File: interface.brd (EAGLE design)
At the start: 101.6 x 38.1 mm, 13 parts, among them U1 LCD-16X2

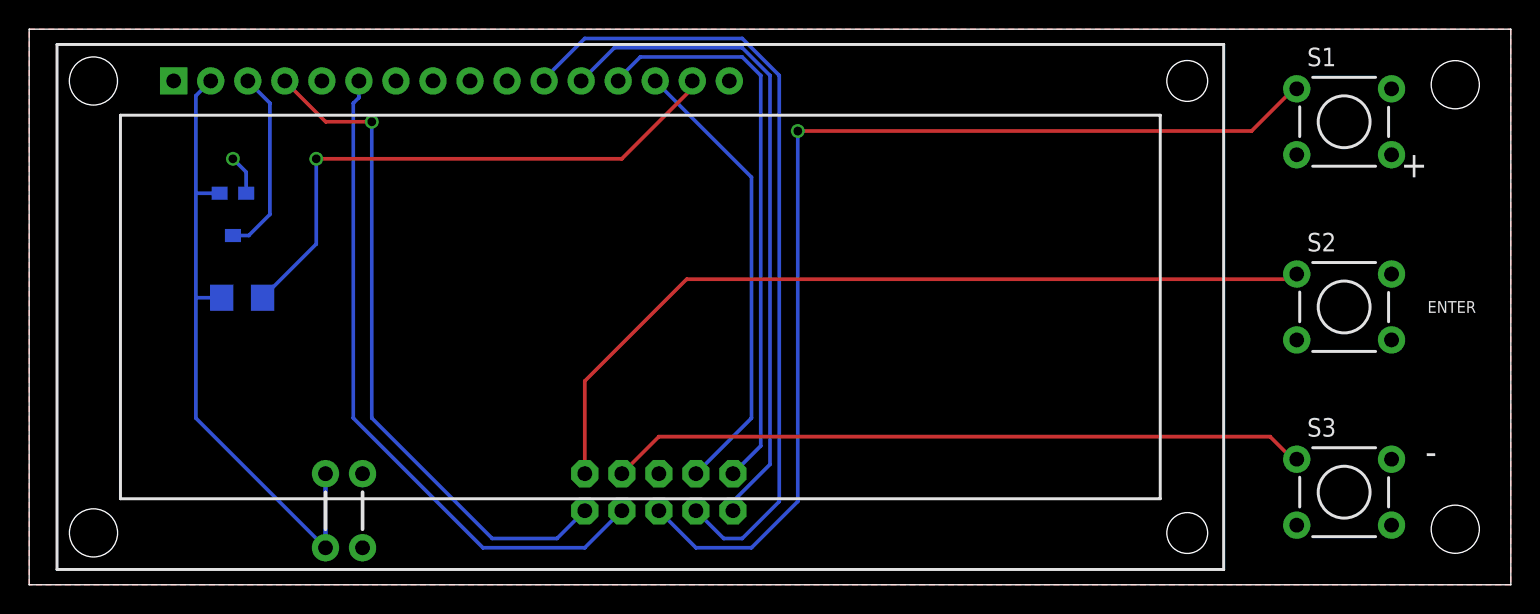
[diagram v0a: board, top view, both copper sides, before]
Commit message: Cleaning up DRC issues
Sparkfun package TRIMPOT_TC33 had issues with silkscreen.  SS from LCD was passing over some pads.  Switched LCD ss to tDocu and cleaned up ss lines on trimpot so they no longer overlapped the pads.
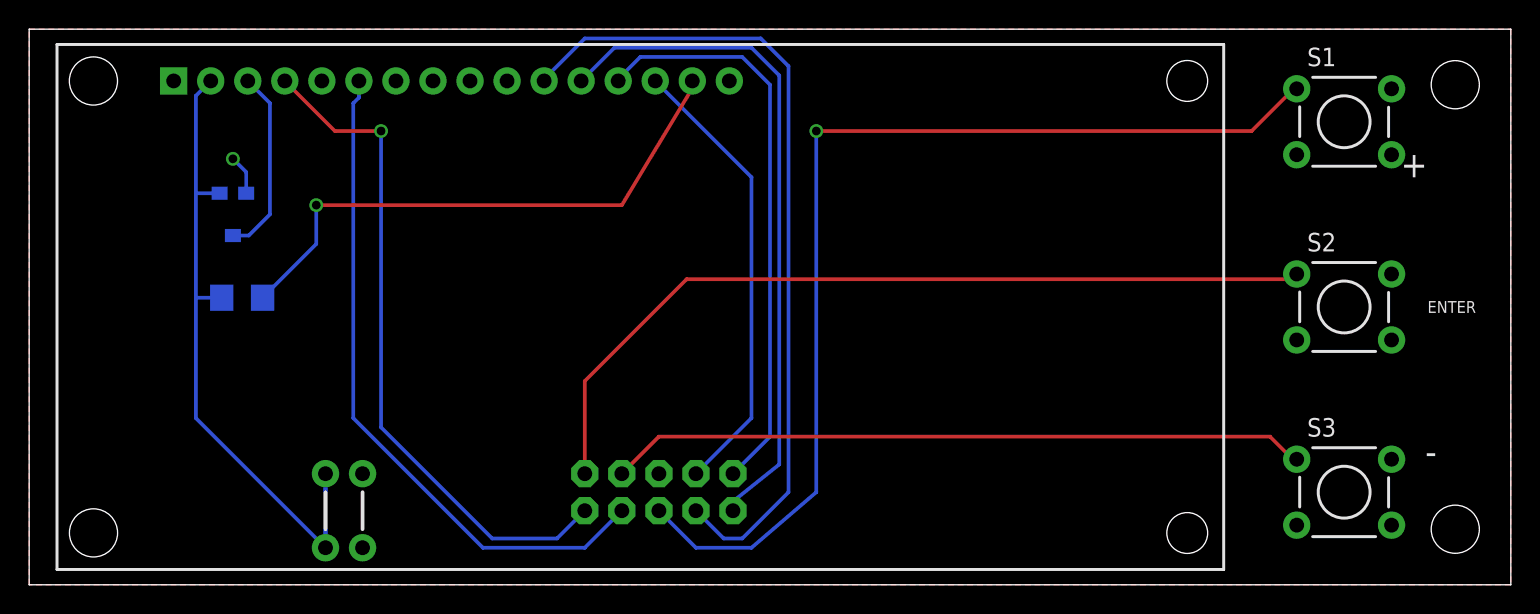
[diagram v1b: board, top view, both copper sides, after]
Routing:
- net LCD_DB4: track 55.2 -> 56.5 mm
- net LCD_DB5: track 45.6 -> 46.7 mm
- net N$1: track 39.3 -> 38.7 mm
- net BTN0: track 72.7 -> 72.2 mm
- net LCD_DB6: track 39.1 -> 39.7 mm
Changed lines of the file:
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@@
 </variantdefs>
 <classes>
-<class number="0" name="default" width="0" drill="0">
+<class number="0" name="default" width="0.254" drill="0.508">
+<clearance class="0" value="0.254"/>
 </class>
 </classes>
@@
 <wire x1="40.39" y1="34.675" x2="41.91" y2="36.195" width="0.254" layer="16"/>
 <wire x1="41.91" y1="36.195" x2="48.895" y2="36.195" width="0.254" layer="16"/>
-<wire x1="48.895" y1="36.195" x2="50.165" y2="34.925" width="0.254" layer="16"/>
-<wire x1="50.165" y1="34.925" x2="50.165" y2="9.525" width="0.254" layer="16"/>
-<wire x1="50.165" y1="9.525" x2="48.26" y2="7.62" width="0.254" layer="16"/>
+<wire x1="48.895" y1="36.195" x2="50.8" y2="34.29" width="0.254" layer="16"/>
+<wire x1="50.8" y1="34.29" x2="50.8" y2="10.16" width="0.254" layer="16"/>
+<wire x1="50.8" y1="10.16" x2="48.26" y2="7.62" width="0.254" layer="16"/>
 </signal>
 <signal name="LCD_RS">
@@
 <wire x1="38.1" y1="5.08" x2="36.195" y2="3.175" width="0.254" layer="16"/>
 <wire x1="36.195" y1="3.175" x2="31.75" y2="3.175" width="0.254" layer="16"/>
-<wire x1="31.75" y1="3.175" x2="23.495" y2="11.43" width="0.254" layer="16"/>
-<wire x1="23.495" y1="11.43" x2="23.495" y2="31.75" width="0.254" layer="16"/>
-<via x="23.495" y="31.75" extent="1-16" drill="0.6"/>
-<wire x1="23.495" y1="31.75" x2="20.33" y2="31.75" width="0.254" layer="1"/>
-<wire x1="20.33" y1="31.75" x2="17.53" y2="34.55" width="0.254" layer="1"/>
+<wire x1="31.75" y1="3.175" x2="24.13" y2="10.795" width="0.254" layer="16"/>
+<wire x1="24.13" y1="10.795" x2="24.13" y2="31.115" width="0.254" layer="16"/>
+<via x="24.13" y="31.115" extent="1-16" drill="0.6"/>
+<wire x1="24.13" y1="31.115" x2="20.965" y2="31.115" width="0.254" layer="1"/>
+<wire x1="20.965" y1="31.115" x2="17.53" y2="34.55" width="0.254" layer="1"/>
 </signal>
 <signal name="LCD_E">
@@
 <wire x1="86.9188" y1="34.0106" x2="86.7156" y2="34.0106" width="0.254" layer="1"/>
 <wire x1="86.7156" y1="34.0106" x2="83.82" y2="31.115" width="0.254" layer="1"/>
-<wire x1="83.82" y1="31.115" x2="52.705" y2="31.115" width="0.254" layer="1"/>
-<via x="52.705" y="31.115" extent="1-16" drill="0.6"/>
-<wire x1="52.705" y1="31.115" x2="52.705" y2="5.715" width="0.254" layer="16"/>
-<wire x1="52.705" y1="5.715" x2="49.53" y2="2.54" width="0.254" layer="16"/>
+<wire x1="83.82" y1="31.115" x2="53.975" y2="31.115" width="0.254" layer="1"/>
+<via x="53.975" y="31.115" extent="1-16" drill="0.6"/>
+<wire x1="53.975" y1="31.115" x2="53.975" y2="6.35" width="0.254" layer="16"/>
+<wire x1="53.975" y1="6.35" x2="49.53" y2="2.54" width="0.254" layer="16"/>
 <wire x1="49.53" y1="2.54" x2="45.72" y2="2.54" width="0.254" layer="16"/>
 <wire x1="45.72" y1="2.54" x2="43.18" y2="5.08" width="0.254" layer="16"/>
@@
 <wire x1="35.31" y1="34.55" x2="35.31" y2="34.675" width="0.254" layer="16"/>
 <wire x1="35.31" y1="34.675" x2="38.1" y2="37.465" width="0.254" layer="16"/>
-<wire x1="38.1" y1="37.465" x2="48.895" y2="37.465" width="0.254" layer="16"/>
-<wire x1="48.895" y1="37.465" x2="51.435" y2="34.925" width="0.254" layer="16"/>
-<wire x1="51.435" y1="34.925" x2="51.435" y2="5.715" width="0.254" layer="16"/>
-<wire x1="51.435" y1="5.715" x2="48.895" y2="3.175" width="0.254" layer="16"/>
+<wire x1="38.1" y1="37.465" x2="50.165" y2="37.465" width="0.254" layer="16"/>
+<wire x1="50.165" y1="37.465" x2="52.07" y2="35.56" width="0.254" layer="16"/>
+<wire x1="52.07" y1="35.56" x2="52.07" y2="6.35" width="0.254" layer="16"/>
+<wire x1="52.07" y1="6.35" x2="48.895" y2="3.175" width="0.254" layer="16"/>
 <wire x1="48.895" y1="3.175" x2="47.625" y2="3.175" width="0.254" layer="16"/>
 <wire x1="47.625" y1="3.175" x2="45.72" y2="5.08" width="0.254" layer="16"/>
@@
 <contactref element="U1" pad="12"/>
 <wire x1="48.26" y1="5.08" x2="48.26" y2="5.715" width="0.254" layer="16"/>
-<wire x1="48.26" y1="5.715" x2="50.8" y2="8.255" width="0.254" layer="16"/>
-<wire x1="50.8" y1="8.255" x2="50.8" y2="34.925" width="0.254" layer="16"/>
-<wire x1="50.8" y1="34.925" x2="48.895" y2="36.83" width="0.254" layer="16"/>
-<wire x1="48.895" y1="36.83" x2="40.13" y2="36.83" width="0.254" layer="16"/>
+<wire x1="48.26" y1="5.715" x2="51.435" y2="8.255" width="0.254" layer="16"/>
+<wire x1="51.435" y1="8.255" x2="51.435" y2="34.925" width="0.254" layer="16"/>
+<wire x1="51.435" y1="34.925" x2="49.53" y2="36.83" width="0.254" layer="16"/>
+<wire x1="49.53" y1="36.83" x2="40.13" y2="36.83" width="0.254" layer="16"/>
 <wire x1="40.13" y1="36.83" x2="37.85" y2="34.55" width="0.254" layer="16"/>
 </signal>
@@
 <contactref element="U1" pad="15"/>
 <wire x1="45.47" y1="34.55" x2="45.47" y2="34.04" width="0.254" layer="1"/>
-<wire x1="45.47" y1="34.04" x2="40.64" y2="29.21" width="0.254" layer="1"/>
-<wire x1="40.64" y1="29.21" x2="19.685" y2="29.21" width="0.254" layer="1"/>
-<via x="19.685" y="29.21" extent="1-16" drill="0.6"/>
-<wire x1="19.685" y1="29.21" x2="19.685" y2="23.365" width="0.254" layer="16"/>
+<wire x1="45.47" y1="34.04" x2="40.64" y2="26.035" width="0.254" layer="1"/>
+<wire x1="40.64" y1="26.035" x2="19.685" y2="26.035" width="0.254" layer="1"/>
+<via x="19.685" y="26.035" extent="1-16" drill="0.6"/>
+<wire x1="19.685" y1="26.035" x2="19.685" y2="23.365" width="0.254" layer="16"/>
 <wire x1="19.685" y1="23.365" x2="16.005" y2="19.685" width="0.254" layer="16"/>
 </signal>

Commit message: Added header for spare pin from 10pin connector.
Added a 2pin header to allow access to the "spare" pin on the 10 pin
header.
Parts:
- added JP4: (no value), SparkFun-Connectors:1X02
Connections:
- net BTN3: now also JP4.2
- net GND: now also JP4.1
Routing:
- net BTN3: track 0.00 -> 23.7 mm
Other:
- board text added: "5V"
- board text added: "GND"
- board text added: "SPARE"
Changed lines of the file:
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@@
 <text x="40.64" y="17.145" size="0.8128" layer="22" rot="SMR270" align="center-left">LCD E</text>
 <text x="38.1" y="23.495" size="0.8128" layer="22" rot="SMR270" align="center-right">BUTTON 1</text>
+<text x="20.32" y="9.525" size="1.016" layer="22" rot="SMR270" align="center-right">5V</text>
+<text x="22.86" y="9.525" size="1.016" layer="22" rot="SMR270" align="center-right">GND</text>
+<text x="64.135" y="2.54" size="0.8128" layer="22" rot="MR0" align="center-right">SPARE</text>
 </plain>
 <attributes>
@@
 <attribute name="VALUE" x="24.13" y="4.445" size="1.27" layer="28" rot="MR0"/>
 </element>
+<element name="JP4" library="SparkFun-Connectors" package="1X02" value="" x="59.69" y="2.54" smashed="yes" rot="MR180">
+<attribute name="VALUE" x="58.42" y="5.715" size="1.27" layer="28" rot="MR180"/>
+</element>
 </elements>
 <signals>
@@
 <signal name="BTN3">
 <contactref element="JP1" pad="5"/>
+<contactref element="JP4" pad="2"/>
+<wire x1="43.18" y1="7.62" x2="45.085" y2="9.525" width="0.254" layer="1"/>
+<wire x1="45.085" y1="9.525" x2="57.785" y2="9.525" width="0.254" layer="1"/>
+<wire x1="57.785" y1="9.525" x2="62.23" y2="2.54" width="0.254" layer="1"/>
 </signal>
 <signal name="LCD_DB7">
@@
 <wire x1="14.88" y1="28.3" x2="13.97" y2="29.21" width="0.254" layer="16"/>
 <contactref element="JP3" pad="1"/>
+<contactref element="JP4" pad="1"/>
 </signal>
 <signal name="+5V">

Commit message: Fixed orientation of screw terminals.
Screw terminals were oriented with receptacle facing inwards towards
the center of the board. Rotated them and performed some pin swaps.

Also added silk to label contrast trim pot on interface board.
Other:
- board text added: "Contrast"
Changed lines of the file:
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@@
 <text x="22.86" y="9.525" size="1.016" layer="22" rot="SMR270" align="center-right">GND</text>
 <text x="64.135" y="2.54" size="0.8128" layer="22" rot="MR0" align="center-right">SPARE</text>
+<text x="13.97" y="22.86" size="0.8128" layer="22" rot="MR0" align="center">Contrast</text>
 </plain>
 <attributes>

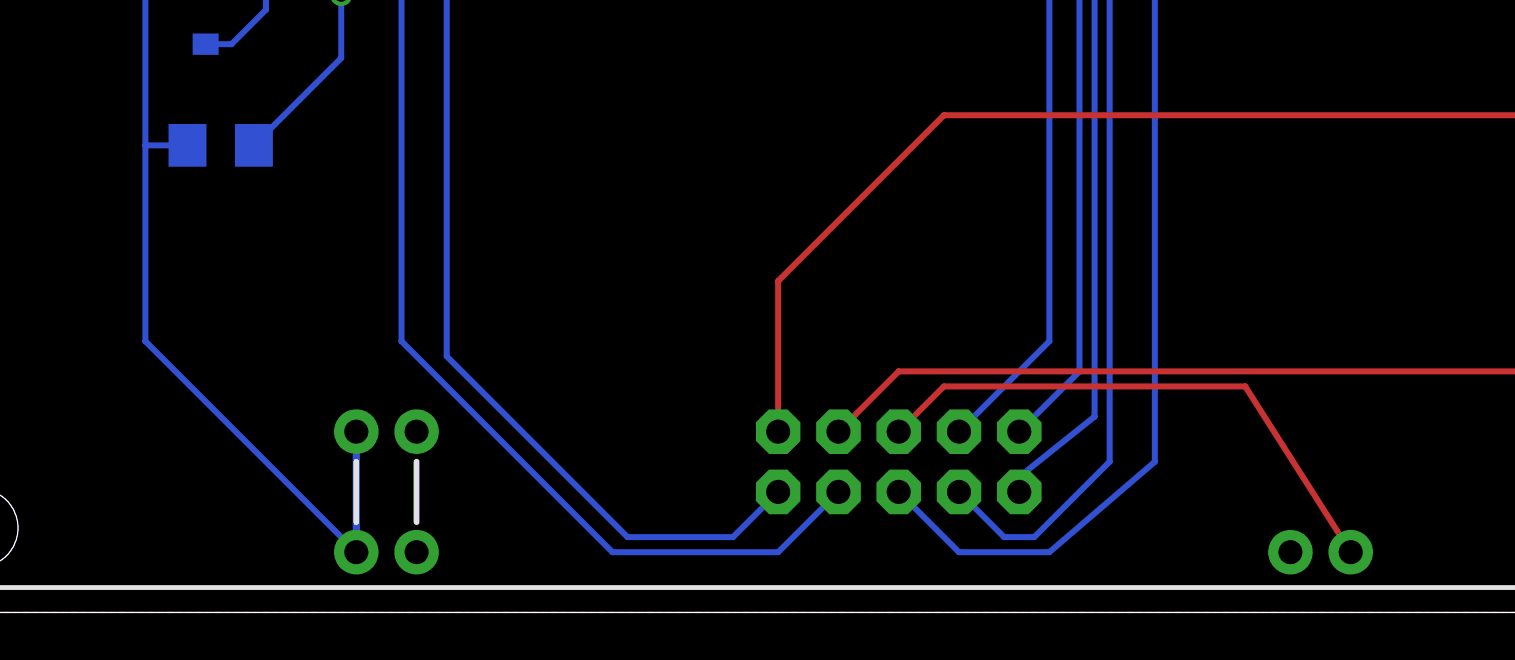
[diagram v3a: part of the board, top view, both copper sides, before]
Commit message: Changed 1 of the aux power connectors to molex polarized header.
Made change for interface and for controller boards
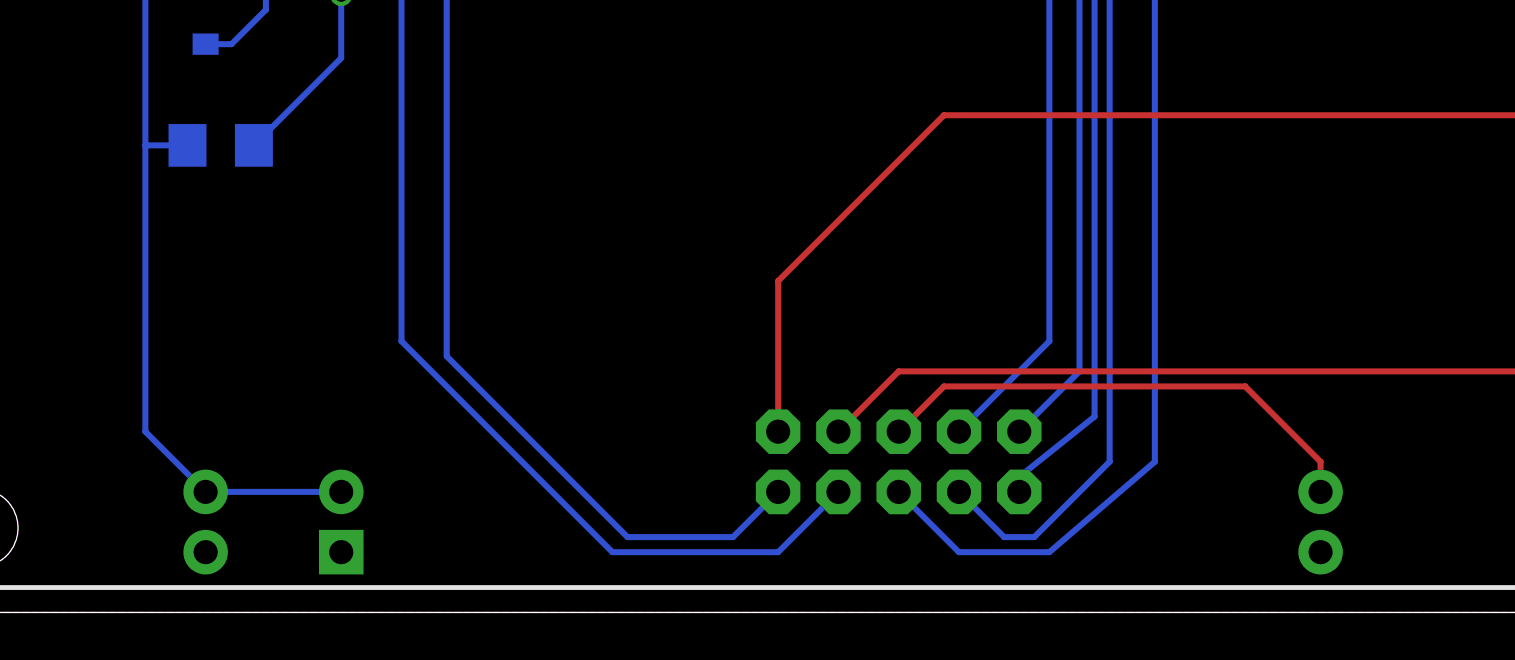
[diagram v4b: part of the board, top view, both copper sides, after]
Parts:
- JP2: device SparkFun-Connectors:1X02 -> SparkFun-Connectors:MOLEX-1X2
- R1: value 6.8 Ohm -> 10 Ohm
- moved JP3 10.2 mm to (14.0, 2.54), turned to 90 degrees
- moved JP2 3.18 mm to (19.7, 2.54), turned to 90 degrees
- moved JP4 1.27 mm to (61.0, 2.54), turned to 90 degrees
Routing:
- net +5V: track 44.6 -> 40.1 mm
- net BTN3: track 23.7 -> 21.2 mm
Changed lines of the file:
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@@
 <text x="96.52" y="8.255" size="1.778" layer="21" rot="MR0">-</text>
 <text x="95.885" y="19.05" size="0.8128" layer="21" align="center-left">ENTER</text>
-<wire x1="20.32" y1="6.35" x2="20.32" y2="3.81" width="0.254" layer="21"/>
-<wire x1="22.86" y1="6.35" x2="22.86" y2="3.81" width="0.254" layer="21"/>
 <text x="38.1" y="21.59" size="0.8128" layer="22" rot="SMR270" align="center">1</text>
 <text x="38.1" y="19.05" size="0.8128" layer="22" rot="SMR270" align="center">2</text>
@@
 <text x="40.64" y="17.145" size="0.8128" layer="22" rot="SMR270" align="center-left">LCD E</text>
 <text x="38.1" y="23.495" size="0.8128" layer="22" rot="SMR270" align="center-right">BUTTON 1</text>
-<text x="20.32" y="9.525" size="1.016" layer="22" rot="SMR270" align="center-right">5V</text>
-<text x="22.86" y="9.525" size="1.016" layer="22" rot="SMR270" align="center-right">GND</text>
-<text x="64.135" y="2.54" size="0.8128" layer="22" rot="MR0" align="center-right">SPARE</text>
+<text x="23.495" y="5.08" size="1.016" layer="22" rot="SMR0" align="center-right">5V</text>
+<text x="23.495" y="2.54" size="1.016" layer="22" rot="SMR0" align="center-right">GND</text>
+<text x="64.77" y="5.08" size="0.8128" layer="22" rot="MR0" align="center-right">SPARE</text>
 <text x="13.97" y="22.86" size="0.8128" layer="22" rot="MR0" align="center">Contrast</text>
+<wire x1="15.24" y1="5.08" x2="17.145" y2="5.08" width="0.254" layer="22"/>
+<wire x1="15.24" y1="2.54" x2="17.145" y2="2.54" width="0.254" layer="22"/>
 </plain>
 <attributes>
@@
 <element name="S2" library="SparkFun-Electromechanical" package="TACTILE-PTH" value="" x="90.17" y="19.05"/>
 <element name="S3" library="SparkFun-Electromechanical" package="TACTILE-PTH" value="" x="90.17" y="6.35"/>
-<element name="JP2" library="SparkFun-Connectors" package="1X02" value="" x="22.86" y="2.54" smashed="yes" rot="MR0">
-<attribute name="VALUE" x="24.13" y="-0.635" size="1.27" layer="28" rot="MR0"/>
-</element>
-<element name="R1" library="SparkFun-Resistors" package="1206" value="6.8 Ohm" x="14.605" y="19.685" smashed="yes" rot="MR180">
+<element name="JP2" library="SparkFun-Connectors" package="MOLEX-1X2" value="" x="19.685" y="2.54" smashed="yes" rot="MR90">
+<attribute name="VALUE" x="16.51" y="1.27" size="1.27" layer="28" rot="MR90"/>
+</element>
+<element name="R1" library="SparkFun-Resistors" package="1206" value="10 Ohm" x="14.605" y="19.685" smashed="yes" rot="MR180">
 <attribute name="NAME" x="13.335" y="18.542" size="0.8128" layer="26" rot="MR180"/>
 </element>
@@
 <element name="U$3" library="SparkFun-Electromechanical" package="STAND-OFF" value="" x="4.406853125" y="34.54639375"/>
 <element name="U$4" library="SparkFun-Electromechanical" package="STAND-OFF" value="" x="4.4115625" y="3.558896875"/>
-<element name="JP3" library="SparkFun-Connectors" package="1X02" value="" x="22.86" y="7.62" smashed="yes" rot="MR0">
-<attribute name="VALUE" x="24.13" y="4.445" size="1.27" layer="28" rot="MR0"/>
-</element>
-<element name="JP4" library="SparkFun-Connectors" package="1X02" value="" x="59.69" y="2.54" smashed="yes" rot="MR180">
-<attribute name="VALUE" x="58.42" y="5.715" size="1.27" layer="28" rot="MR180"/>
+<element name="JP3" library="SparkFun-Connectors" package="1X02" value="" x="13.97" y="2.54" smashed="yes" rot="MR90">
+<attribute name="VALUE" x="10.795" y="1.27" size="1.27" layer="28" rot="MR90"/>
+</element>
+<element name="JP4" library="SparkFun-Connectors" package="1X02" value="" x="60.96" y="2.54" smashed="yes" rot="MR90">
+<attribute name="VALUE" x="57.785" y="1.27" size="1.27" layer="28" rot="MR90"/>
 </element>
 </elements>
@@
 <wire x1="43.18" y1="7.62" x2="45.085" y2="9.525" width="0.254" layer="1"/>
 <wire x1="45.085" y1="9.525" x2="57.785" y2="9.525" width="0.254" layer="1"/>
-<wire x1="57.785" y1="9.525" x2="62.23" y2="2.54" width="0.254" layer="1"/>
+<wire x1="57.785" y1="9.525" x2="60.96" y2="6.35" width="0.254" layer="1"/>
+<wire x1="60.96" y1="6.35" x2="60.96" y2="5.08" width="0.254" layer="1"/>
 </signal>
 <signal name="LCD_DB7">
@@
 <wire x1="11.43" y1="26.85" x2="11.43" y2="33.53" width="0.254" layer="16"/>
 <wire x1="11.43" y1="33.53" x2="12.45" y2="34.55" width="0.254" layer="16"/>
-<wire x1="20.32" y1="2.54" x2="11.43" y2="11.43" width="0.254" layer="16"/>
-<wire x1="11.43" y1="11.43" x2="11.43" y2="19.685" width="0.254" layer="16"/>
 <wire x1="11.43" y1="19.685" x2="11.43" y2="26.85" width="0.254" layer="16"/>
 <wire x1="13.205" y1="19.685" x2="11.43" y2="19.685" width="0.254" layer="16"/>
 <contactref element="JP3" pad="2"/>
-<wire x1="20.32" y1="7.62" x2="20.32" y2="2.54" width="0.3048" layer="16"/>
+<wire x1="13.97" y1="5.08" x2="19.685" y2="5.08" width="0.254" layer="16"/>
+<wire x1="11.43" y1="19.685" x2="11.43" y2="7.62" width="0.254" layer="16"/>
+<wire x1="11.43" y1="7.62" x2="13.97" y2="5.08" width="0.254" layer="16"/>
 </signal>
 <signal name="LCD_VO">

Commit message: Updated some layout, added logo
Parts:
- added U$5: MN-LOGO, Mikes-Aesthetics:MN-LOGO
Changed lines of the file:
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@@
 <layer number="20" name="Dimension" color="15" fill="1" visible="yes" active="yes"/>
 <layer number="21" name="tPlace" color="7" fill="1" visible="yes" active="yes"/>
-<layer number="22" name="bPlace" color="7" fill="1" visible="yes" active="yes"/>
+<layer number="22" name="bPlace" color="13" fill="1" visible="yes" active="yes"/>
 <layer number="23" name="tOrigins" color="15" fill="1" visible="yes" active="yes"/>
 <layer number="24" name="bOrigins" color="15" fill="1" visible="yes" active="yes"/>
@@
 <attribute name="VALUE" x="57.785" y="1.27" size="1.27" layer="28" rot="MR90"/>
 </element>
+<element name="U$5" library="Mikes-Aesthetics" package="MN-LOGO" value="MN-LOGO" x="6.985" y="10.795" rot="MR0"/>
 </elements>
 <signals>
